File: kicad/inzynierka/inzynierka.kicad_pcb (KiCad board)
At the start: 2 copper layers, 170 x 175 mm, 36 parts

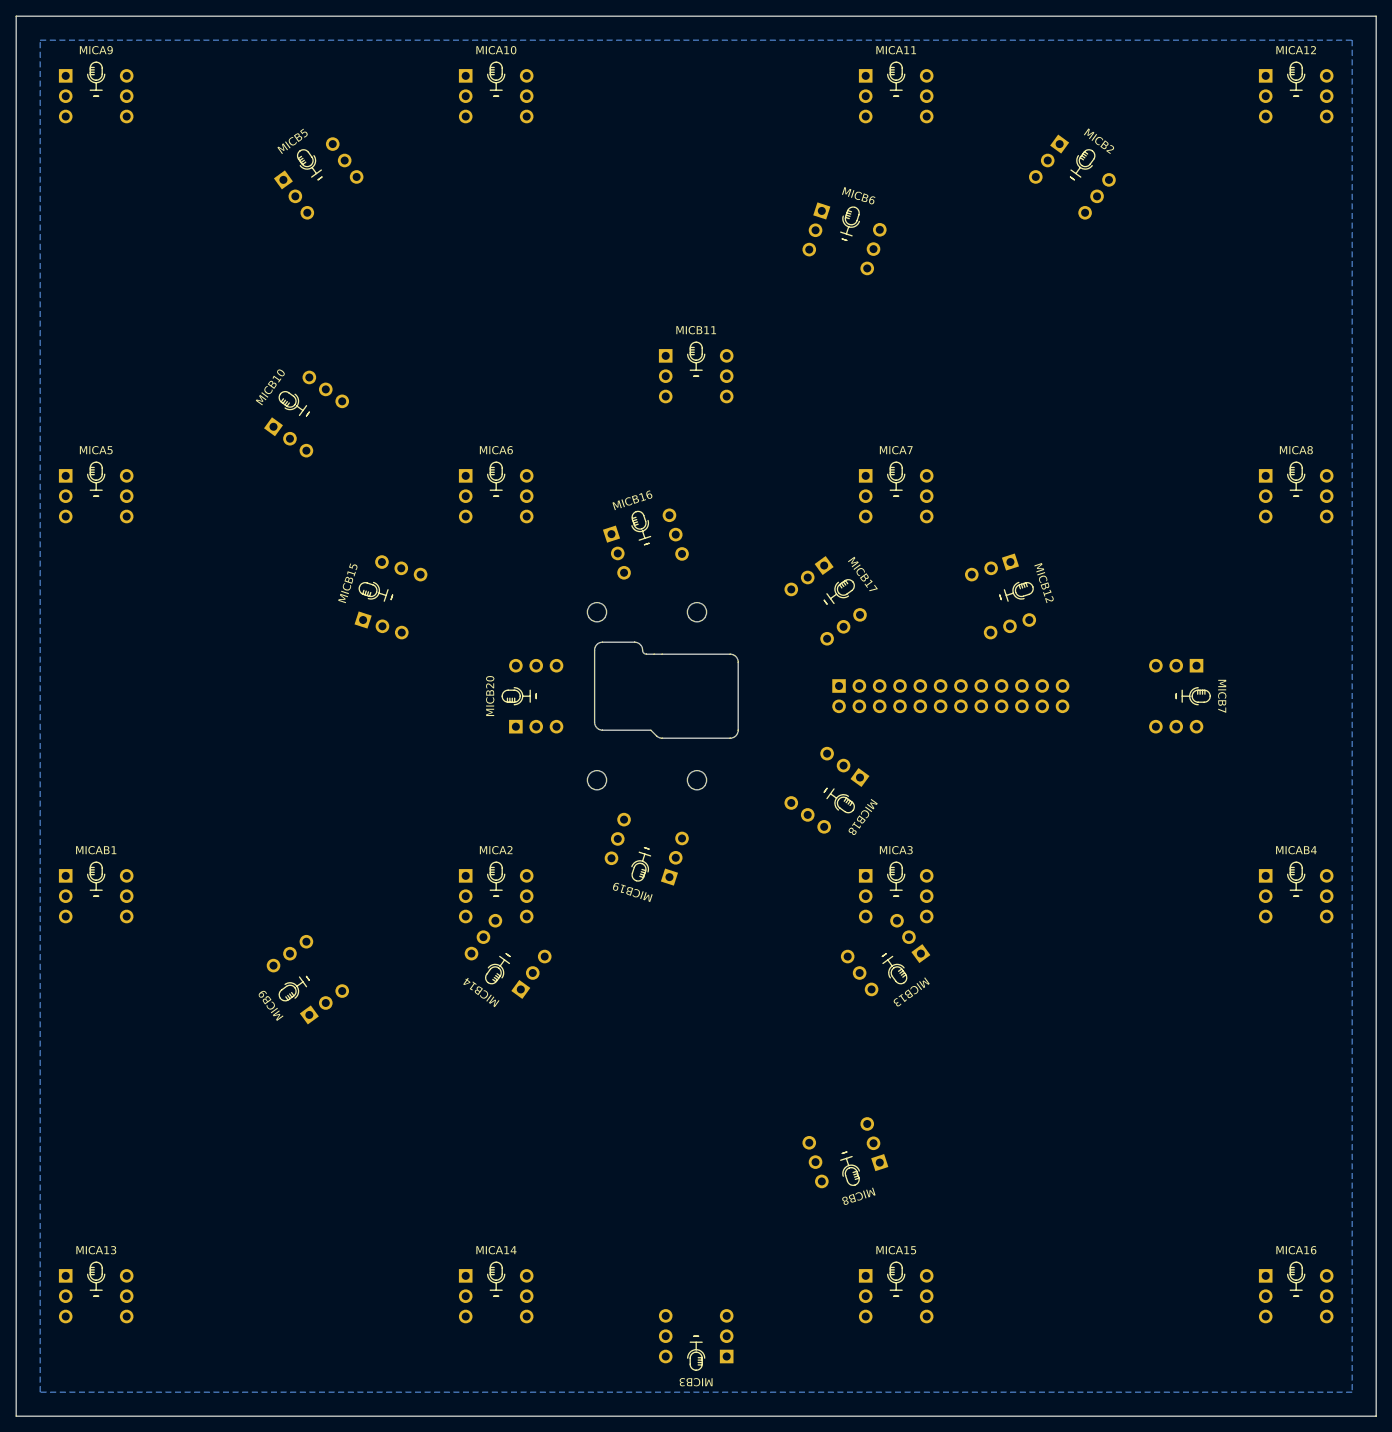
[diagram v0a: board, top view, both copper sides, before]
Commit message: Dodanie trasowania dla CLK1 i linii danych + rozpoczęcie trasowania CLK2
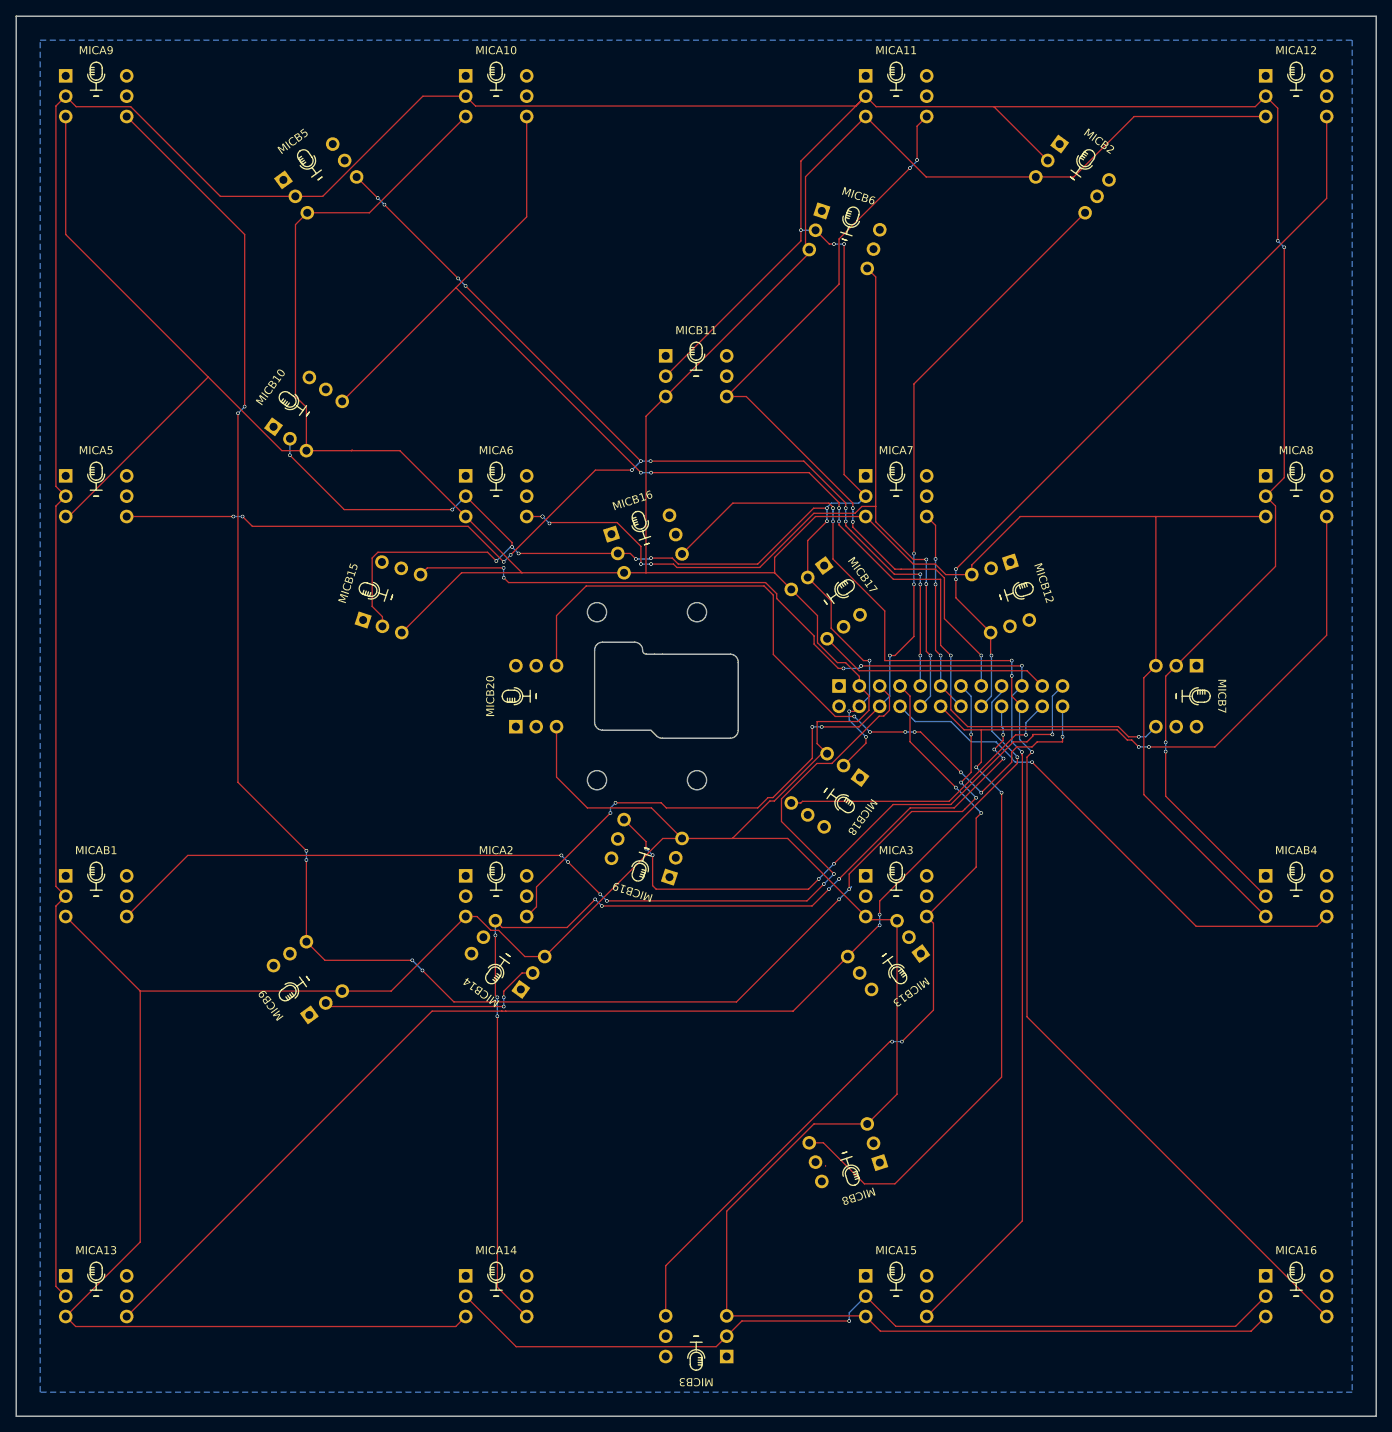
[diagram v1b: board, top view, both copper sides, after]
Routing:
- net CLK1: track 0.00 -> 900.6 mm
- net CLK2: track 0.00 -> 813.7 mm, vias 0 -> 22
- net D9: track 0.00 -> 228.3 mm, vias 0 -> 11
- net D5: track 0.00 -> 178.5 mm, vias 0 -> 16
- net D15: track 0.00 -> 169.9 mm, vias 0 -> 6
- net D16: track 0.00 -> 158.5 mm, vias 0 -> 5
- net D13: track 0.00 -> 153.3 mm, vias 0 -> 3
- net D8: track 0.00 -> 147.6 mm, vias 0 -> 4
- net D10: track 0.00 -> 139.4 mm, vias 0 -> 5
- net D2: track 0.00 -> 132.3 mm, vias 0 -> 7
- net D14: track 0.00 -> 132.0 mm, vias 0 -> 10
- net D1: track 0.00 -> 129.1 mm, vias 0 -> 6
- net D6: track 0.00 -> 110.5 mm, vias 0 -> 8
- net D3: track 0.00 -> 100.9 mm, vias 0 -> 4
- net D11: track 0.00 -> 99.1 mm, vias 0 -> 5
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
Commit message: Dokończenie trasowania CLK2
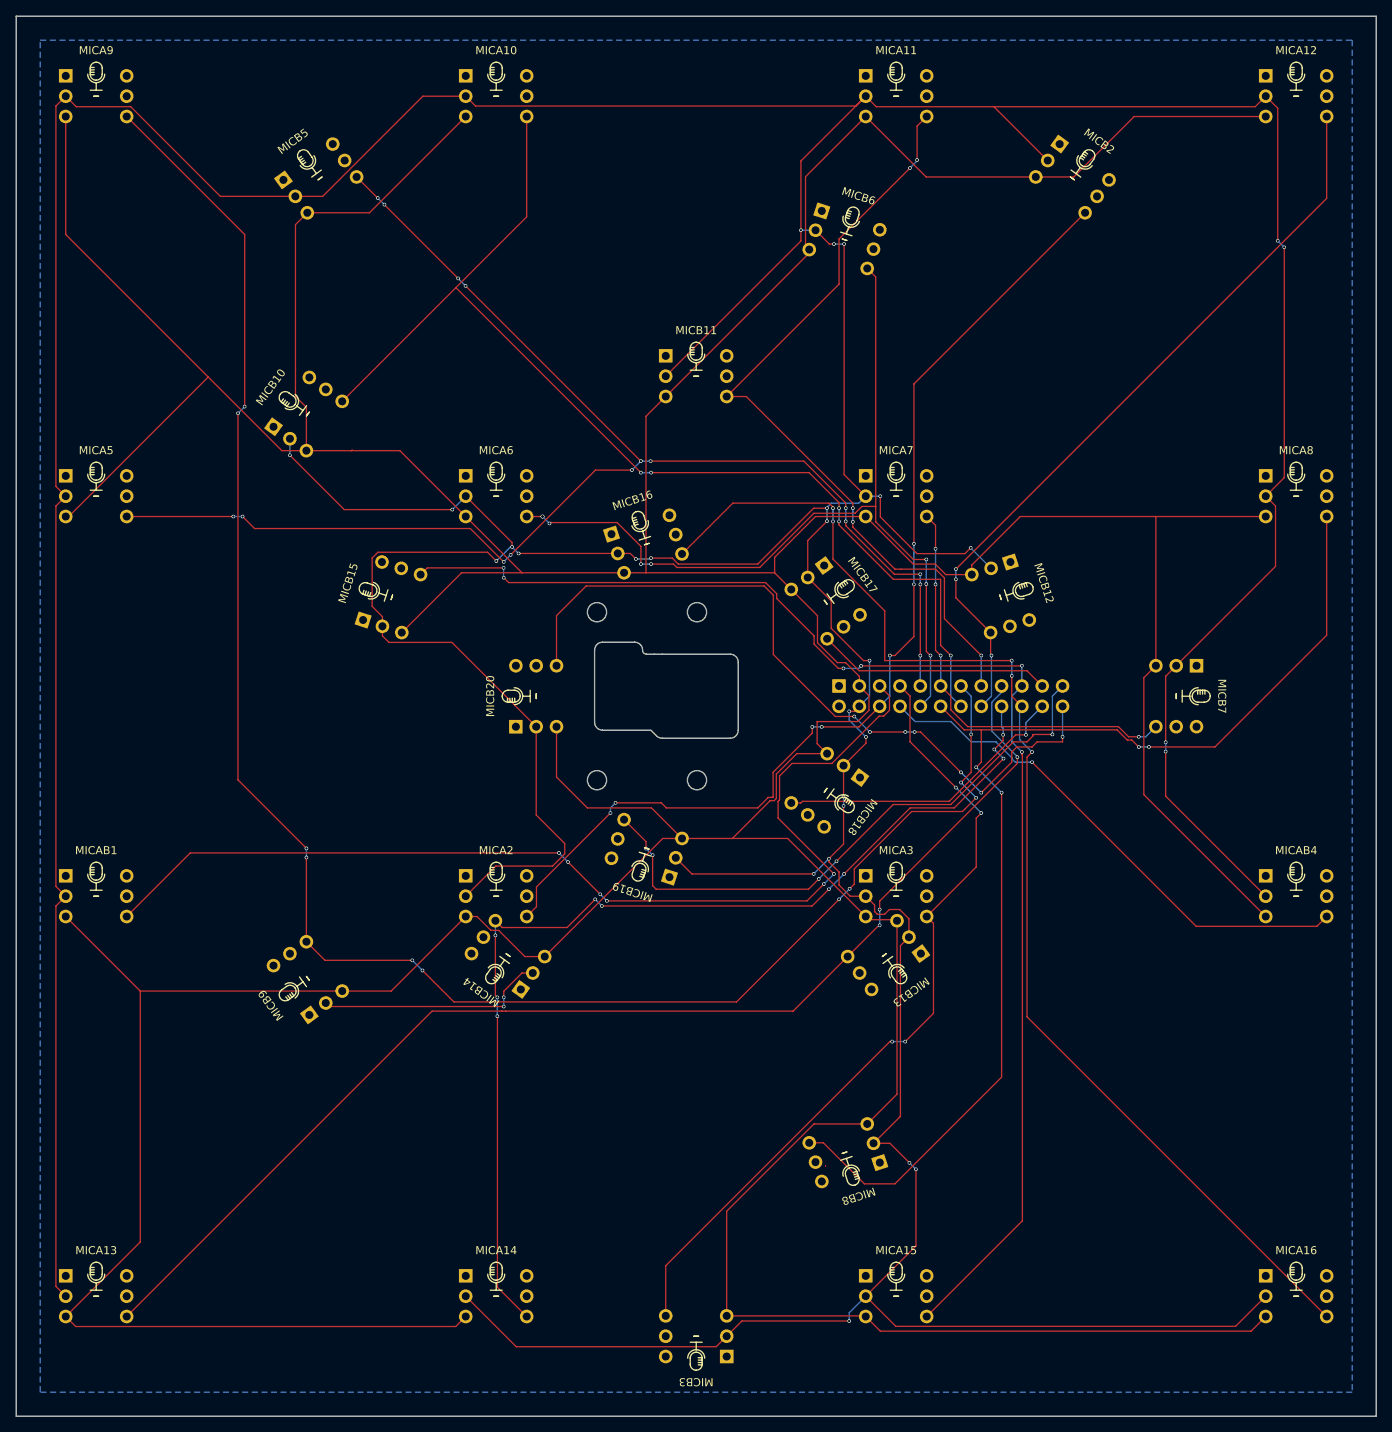
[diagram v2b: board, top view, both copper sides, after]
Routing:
- net CLK2: track 813.7 -> 995.8 mm, vias 22 -> 30
- net D1: track 129.1 -> 131.5 mm
- net CLK1: track 900.6 -> 902.4 mm
- net D9: track 228.3 -> 227.5 mm

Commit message: Podłączenie L/R na głośnikach do GND
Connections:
- MICA10 pad 1: +3.3V -> GND
- MICA11 pad 1: +3.3V -> GND
- MICA12 pad 1: +3.3V -> GND
- MICA13 pad 1: +3.3V -> GND
- MICA14 pad 1: +3.3V -> GND
- MICA15 pad 1: +3.3V -> GND
- MICA16 pad 1: +3.3V -> GND
- MICA2 pad 1: +3.3V -> GND
- MICA3 pad 1: +3.3V -> GND
- MICA5 pad 1: +3.3V -> GND
- MICA6 pad 1: +3.3V -> GND
- MICA7 pad 1: +3.3V -> GND
- MICA8 pad 1: +3.3V -> GND
- MICA9 pad 1: +3.3V -> GND
- MICAB1 pad 1: +3.3V -> GND
- MICAB4 pad 1: +3.3V -> GND
- MICB10 pad 1: +3.3V -> GND
- MICB11 pad 1: +3.3V -> GND
- MICB12 pad 1: +3.3V -> GND
- MICB13 pad 1: +3.3V -> GND
- MICB14 pad 1: +3.3V -> GND
- MICB15 pad 1: +3.3V -> GND
- MICB16 pad 1: +3.3V -> GND
- MICB17 pad 1: +3.3V -> GND
- MICB18 pad 1: +3.3V -> GND
- MICB19 pad 1: +3.3V -> GND
- MICB2 pad 1: +3.3V -> GND
- MICB20 pad 1: +3.3V -> GND
- MICB3 pad 1: +3.3V -> GND
- MICB5 pad 1: +3.3V -> GND
- MICB6 pad 1: +3.3V -> GND
- MICB7 pad 1: +3.3V -> GND
- MICB8 pad 1: +3.3V -> GND
- MICB9 pad 1: +3.3V -> GND
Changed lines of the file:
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@@
 			(layers "*.Cu" "*.Mask")
 			(remove_unused_layers no)
-			(net 5 "+3.3V")
+			(net 2 "GND")
 			(pinfunction "L/R")
 			(pintype "input")
@@
 			(layers "*.Cu" "*.Mask")
 			(remove_unused_layers no)
-			(net 5 "+3.3V")
+			(net 2 "GND")
 			(pinfunction "L/R")
 			(pintype "input")
@@
 			(layers "*.Cu" "*.Mask")
 			(remove_unused_layers no)
-			(net 5 "+3.3V")
+			(net 2 "GND")
 			(pinfunction "L/R")
 			(pintype "input")
@@
 			(layers "*.Cu" "*.Mask")
 			(remove_unused_layers no)
-			(net 5 "+3.3V")
+			(net 2 "GND")
 			(pinfunction "L/R")
 			(pintype "input")
@@
 			(layers "*.Cu" "*.Mask")
 			(remove_unused_layers no)
-			(net 5 "+3.3V")
+			(net 2 "GND")
 			(pinfunction "L/R")
 			(pintype "input")
@@
 			(layers "*.Cu" "*.Mask")
 			(remove_unused_layers no)
-			(net 5 "+3.3V")
+			(net 2 "GND")
 			(pinfunction "L/R")
 			(pintype "input")
@@
 			(layers "*.Cu" "*.Mask")
 			(remove_unused_layers no)
-			(net 5 "+3.3V")
+			(net 2 "GND")
 			(pinfunction "L/R")
 			(pintype "input")
@@
 			(layers "*.Cu" "*.Mask")
 			(remove_unused_layers no)
-			(net 5 "+3.3V")
+			(net 2 "GND")
 			(pinfunction "L/R")
 			(pintype "input")
@@
 			(layers "*.Cu" "*.Mask")
 			(remove_unused_layers no)
-			(net 5 "+3.3V")
+			(net 2 "GND")
 			(pinfunction "L/R")
 			(pintype "input")
@@
 			(layers "*.Cu" "*.Mask")
 			(remove_unused_layers no)
-			(net 5 "+3.3V")
+			(net 2 "GND")
 			(pinfunction "L/R")
 			(pintype "input")
@@
 			(layers "*.Cu" "*.Mask")
 			(remove_unused_layers no)
-			(net 5 "+3.3V")
+			(net 2 "GND")
 			(pinfunction "L/R")
 			(pintype "input")
@@
 			(layers "*.Cu" "*.Mask")
 			(remove_unused_layers no)
-			(net 5 "+3.3V")
+			(net 2 "GND")
 			(pinfunction "L/R")
 			(pintype "input")
@@
 			(layers "*.Cu" "*.Mask")
 			(remove_unused_layers no)
-			(net 5 "+3.3V")
+			(net 2 "GND")
 			(pinfunction "L/R")
 			(pintype "input")
@@
 			(layers "*.Cu" "*.Mask")
 			(remove_unused_layers no)
-			(net 5 "+3.3V")
+			(net 2 "GND")
 			(pinfunction "L/R")
 			(pintype "input")
@@
 			(layers "*.Cu" "*.Mask")
 			(remove_unused_layers no)
-			(net 5 "+3.3V")
+			(net 2 "GND")
 			(pinfunction "L/R")
 			(pintype "input")
@@
 			(layers "*.Cu" "*.Mask")
 			(remove_unused_layers no)
-			(net 5 "+3.3V")
+			(net 2 "GND")
 			(pinfunction "L/R")
 			(pintype "input")
@@
 			(layers "*.Cu" "*.Mask")
 			(remove_unused_layers no)
-			(net 5 "+3.3V")
+			(net 2 "GND")
 			(pinfunction "L/R")
 			(pintype "input")
@@
 			(layers "*.Cu" "*.Mask")
 			(remove_unused_layers no)
-			(net 5 "+3.3V")
+			(net 2 "GND")
 			(pinfunction "L/R")
 			(pintype "input")
@@
 			(layers "*.Cu" "*.Mask")
 			(remove_unused_layers no)
-			(net 5 "+3.3V")
+			(net 2 "GND")
 			(pinfunction "L/R")
 			(pintype "input")
@@
 			(layers "*.Cu" "*.Mask")
 			(remove_unused_layers no)
-			(net 5 "+3.3V")
+			(net 2 "GND")
 			(pinfunction "L/R")
 			(pintype "input")
@@
 			(layers "*.Cu" "*.Mask")
 			(remove_unused_layers no)
-			(net 5 "+3.3V")
+			(net 2 "GND")
 			(pinfunction "L/R")
 			(pintype "input")
@@
 			(layers "*.Cu" "*.Mask")
 			(remove_unused_layers no)
-			(net 5 "+3.3V")
+			(net 2 "GND")
 			(pinfunction "L/R")
 			(pintype "input")
@@
 			(layers "*.Cu" "*.Mask")
 			(remove_unused_layers no)
-			(net 5 "+3.3V")
+			(net 2 "GND")
 			(pinfunction "L/R")
 			(pintype "input")
@@
 			(layers "*.Cu" "*.Mask")
 			(remove_unused_layers no)
-			(net 5 "+3.3V")
+			(net 2 "GND")
 			(pinfunction "L/R")
 			(pintype "input")
@@
 			(layers "*.Cu" "*.Mask")
 			(remove_unused_layers no)
-			(net 5 "+3.3V")
+			(net 2 "GND")
 			(pinfunction "L/R")
 			(pintype "input")
@@
 			(layers "*.Cu" "*.Mask")
 			(remove_unused_layers no)
-			(net 5 "+3.3V")
+			(net 2 "GND")
 			(pinfunction "L/R")
 			(pintype "input")
@@
 			(layers "*.Cu" "*.Mask")
 			(remove_unused_layers no)
-			(net 5 "+3.3V")
+			(net 2 "GND")
 			(pinfunction "L/R")
 			(pintype "input")
@@
 			(layers "*.Cu" "*.Mask")
 			(remove_unused_layers no)
-			(net 5 "+3.3V")
+			(net 2 "GND")
 			(pinfunction "L/R")
 			(pintype "input")
@@
 			(layers "*.Cu" "*.Mask")
 			(remove_unused_layers no)
-			(net 5 "+3.3V")
+			(net 2 "GND")
 			(pinfunction "L/R")
 			(pintype "input")
@@
 			(layers "*.Cu" "*.Mask")
 			(remove_unused_layers no)
-			(net 5 "+3.3V")
+			(net 2 "GND")
 			(pinfunction "L/R")
 			(pintype "input")
@@
 			(layers "*.Cu" "*.Mask")
 			(remove_unused_layers no)
-			(net 5 "+3.3V")
+			(net 2 "GND")
 			(pinfunction "L/R")
 			(pintype "input")
@@
 			(layers "*.Cu" "*.Mask")
 			(remove_unused_layers no)
-			(net 5 "+3.3V")
+			(net 2 "GND")
 			(pinfunction "L/R")
 			(pintype "input")
@@
 			(layers "*.Cu" "*.Mask")
 			(remove_unused_layers no)
-			(net 5 "+3.3V")
+			(net 2 "GND")
 			(pinfunction "L/R")
 			(pintype "input")
@@
 			(layers "*.Cu" "*.Mask")
 			(remove_unused_layers no)
-			(net 5 "+3.3V")
+			(net 2 "GND")
 			(pinfunction "L/R")
 			(pintype "input")

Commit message: Dokończenie trasowania 3.3V
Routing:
- net +3.3V: track 0.00 -> 1149.9 mm, vias 0 -> 38
- net CLK2: track 995.8 -> 1082.1 mm, vias 30 -> 31
- net CLK1: track 902.4 -> 913.7 mm
- net D6: track 110.5 -> 112.1 mm
- net D5: track 178.5 -> 180.0 mm
- net D14: track 132.0 -> 132.9 mm, vias 10 -> 9
- net D9: track 227.5 -> 228.0 mm
